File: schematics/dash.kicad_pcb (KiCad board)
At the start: 2 copper layers, 29 parts, among them J1 BATT_CONN, J2 EXTERNAL_TRIGGER, J3 USB_OTG, SW1 SW_Push, U1 ESP-12E, U2 ch340g, U3 MCP73833, U4 HT7333, Y1 12Mhz

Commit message: [add] Shitty design to start with
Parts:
- C1, C2, C3, C4, C5, C6, C7, C9, J1, R3: moved to B.Cu
- D3: value LED_Small -> LED
- J2: value EXTERNAL_TRIGGER -> EXT_TRIG
- moved C4 59.6 mm to (129.6, 102.8)
- moved Y1 49.3 mm to (136.6, 119.0), turned to 180 degrees
- moved SW1 43.9 mm to (143.0, 113.2), turned to 90 degrees
- moved C3 38.4 mm to (131.2, 118.8), turned to 270 degrees
- moved C9 30.2 mm to (154.9, 119.8), turned to 180 degrees
- moved U2 25.0 mm to (136.2, 109.8), turned to 270 degrees
- moved J1 23.8 mm to (164.7, 112.2)
- moved C7 22.4 mm to (158.9, 109.5)
- moved R5 21.3 mm to (168.8, 98.6), turned to 180 degrees
- moved R8 20.5 mm to (160.8, 121.4)
- moved C6 20.3 mm to (136.4, 109.0), turned to 90 degrees
- moved D3 20.1 mm to (129.7, 98.0), turned to 180 degrees
- moved D2 19.4 mm to (129.6, 100.5), turned to 180 degrees
- moved D1 19.0 mm to (129.6, 102.9), turned to 180 degrees
- moved C1 18.4 mm to (158.9, 112.9), turned to 180 degrees
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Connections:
- net /USB_VCC renamed +5V
- net /VCC renamed +3V3
- R3 pad 1: Net-(R3-Pad1) -> GND
- R3 pad 2: GND -> Net-(R3-Pad2)
- R4 pad 1: GND -> Net-(D3-Pad1)
- R4 pad 2: Net-(D3-Pad1) -> GND
- U3 pad 6: Net-(R3-Pad1) -> Net-(R3-Pad2)
- U3 pad 9: Net-(C1-Pad1) -> Net-(U3-Pad9)
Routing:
- net /WAKE: track 0.00 -> 40.2 mm, vias 0 -> 2
- net Net-(C1-Pad1): track 0.00 -> 35.9 mm, vias 0 -> 1
- net /CH_PD: track 0.00 -> 31.2 mm, vias 0 -> 4
- net +5V: track 0.00 -> 26.9 mm, vias 0 -> 2
- net Net-(D3-Pad2): track 0.00 -> 24.1 mm, vias 0 -> 2
- net /GPIO0: track 0.00 -> 23.2 mm, vias 0 -> 2
- net GND: track 0.00 -> 20.6 mm, vias 0 -> 4
- net Net-(C2-Pad1): track 0.00 -> 18.2 mm, vias 0 -> 3
- net (no net): track 0.00 -> 15.2 mm
- net Net-(C3-Pad1): track 0.00 -> 8.64 mm, vias 0 -> 1
- net +3V3: track 0.00 -> 8.44 mm, vias 0 -> 1
- net Net-(R3-Pad2): track 0.00 -> 7.55 mm, vias 0 -> 1
- net /D-: track 0.00 -> 6.20 mm, vias 0 -> 2
- net /GPIO2: track 0.00 -> 5.35 mm
- net Net-(R1-Pad2): track 0.00 -> 4.95 mm
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- added copper zone on F.Cu, net +3V3
- added copper zone on B.Cu, net GND
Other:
- board outline added: 50 x 30 mm

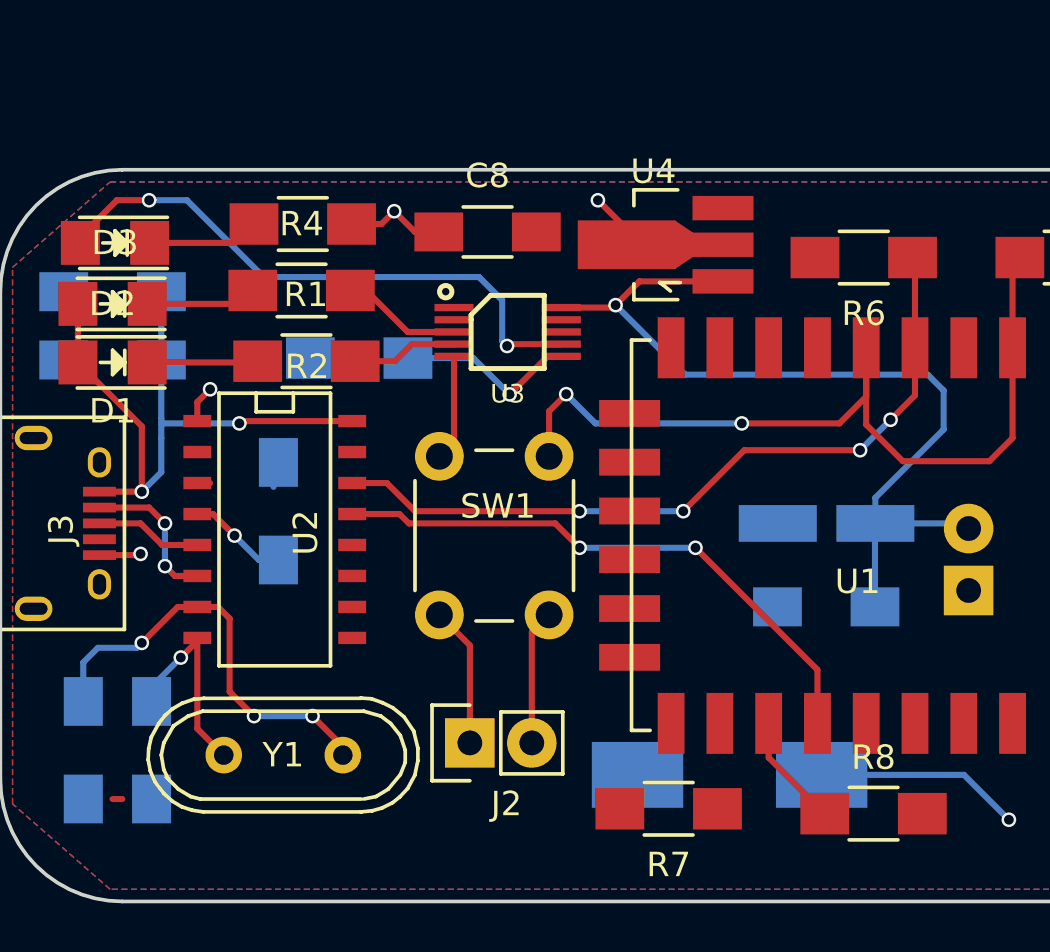
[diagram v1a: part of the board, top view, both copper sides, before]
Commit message: [enh] Change crystal placement and size
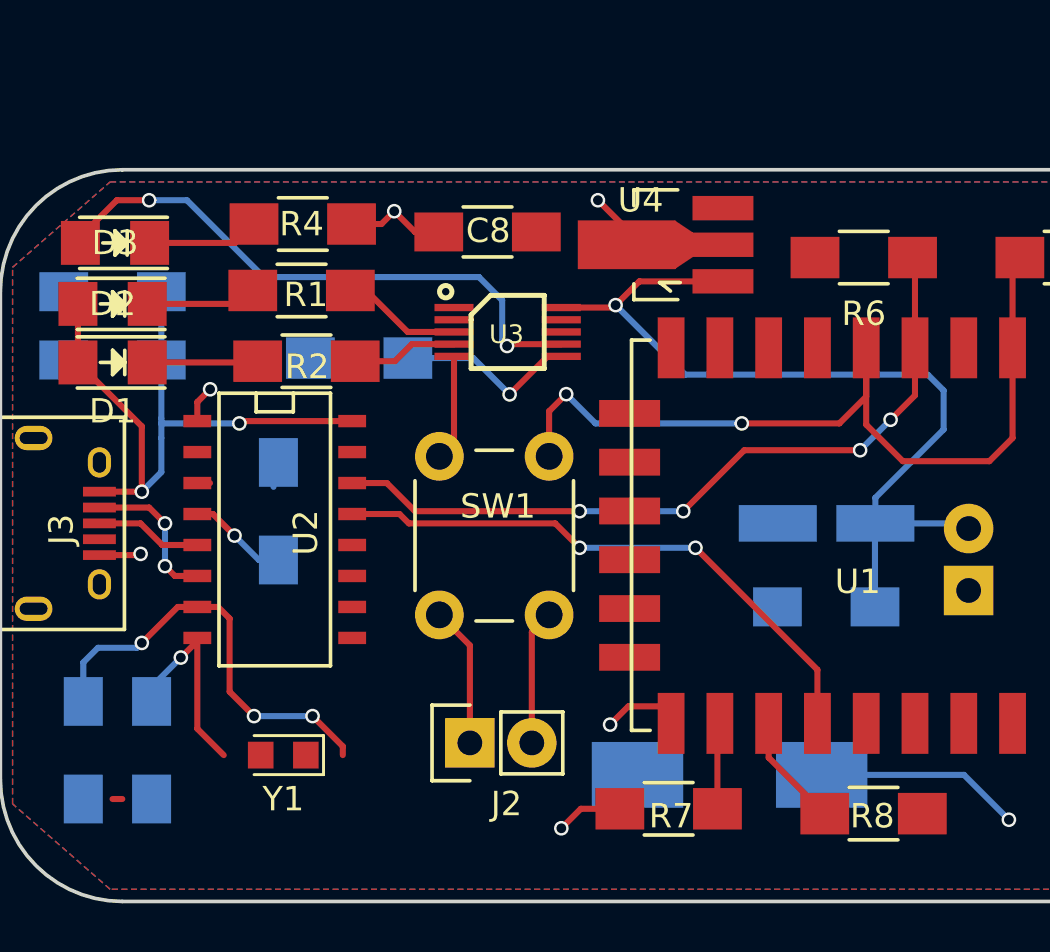
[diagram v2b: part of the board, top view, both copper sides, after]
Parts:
- J2: value EXT_TRIG -> EXTERNAL_TRIGGER
- Y1: footprint Crystals:Crystal_HC49-U_Vertical -> Crystals:Crystal_SMD_2012-2pin_2.0x1.2mm_HandSoldering
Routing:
- net GND: track 20.6 -> 26.1 mm, vias 4 -> 6
- net /GPIO15: track 0.14 -> 4.38 mm

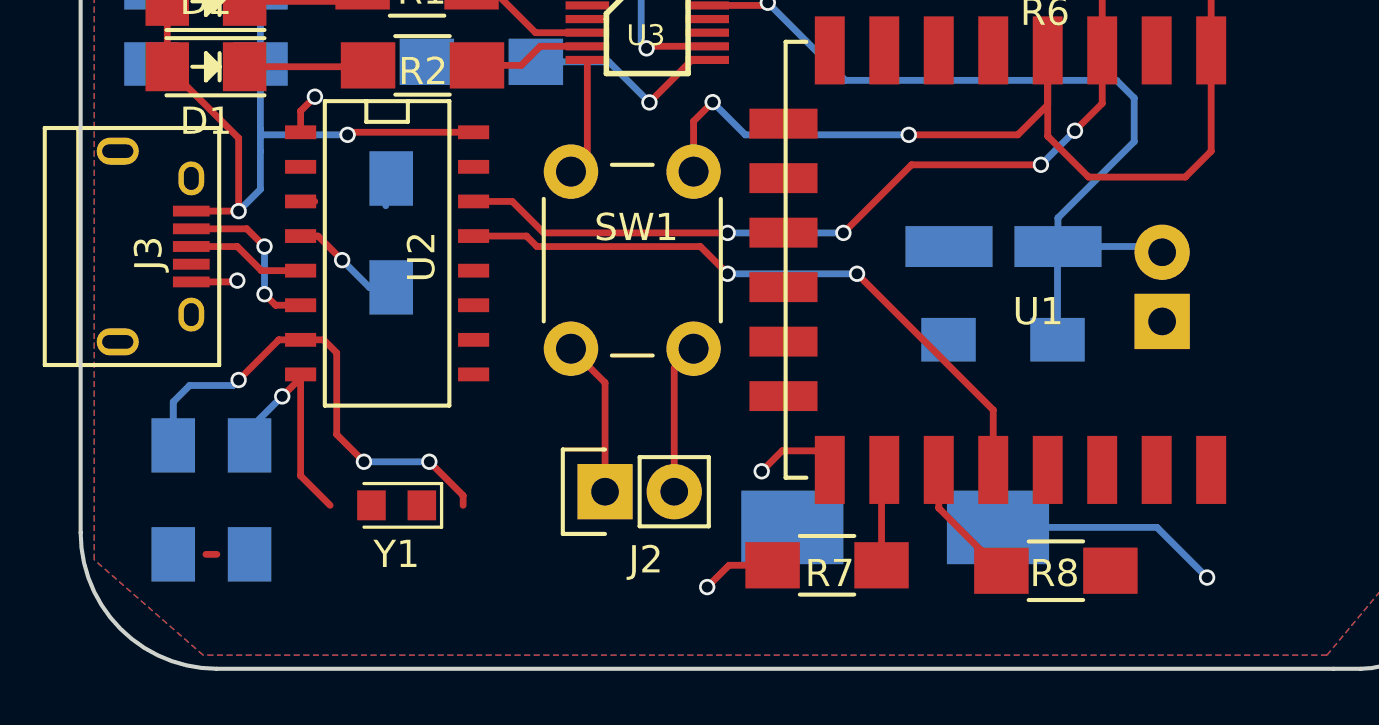
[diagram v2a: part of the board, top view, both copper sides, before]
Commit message: [add] TX/RX wiring to the ESP-12
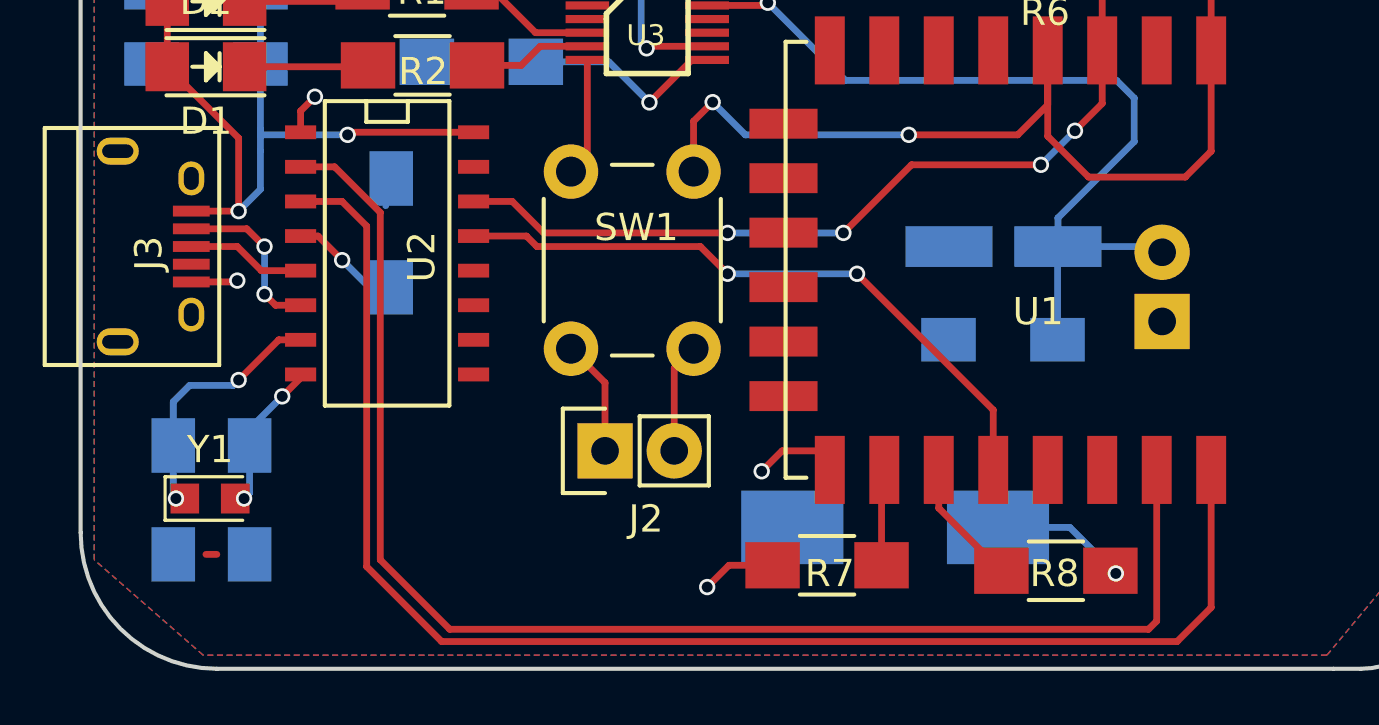
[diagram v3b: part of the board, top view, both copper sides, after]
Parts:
- moved Y1 6.85 mm to (129.8, 118.8), turned to 0 degrees
- moved J2 1.50 mm to (144.2, 117.0)
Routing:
- net /TXD: track 0.52 -> 54.2 mm
- net /RXD: track 0.00 -> 52.3 mm
- net Net-(C2-Pad1): track 18.2 -> 10.0 mm, vias 3 -> 2
- net +3V3: track 8.44 -> 5.27 mm
- net Net-(C3-Pad1): track 8.64 -> 5.89 mm, vias 1 -> 2
- net GND: track 26.1 -> 24.6 mm
- net /WAKE: track 40.2 -> 38.7 mm
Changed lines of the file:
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@@
   (general
     (links 68)
-    (no_connects 15)
+    (no_connects 12)
     (area 124.924999 94.924999 175.075001 125.075001)
     (thickness 1.6)
     (drawings 10)
-    (tracks 182)
+    (tracks 196)
     (zones 0)
     (modules 29)
@@
   )
   (module Pin_Headers:Pin_Header_Straight_1x02 (layer F.Cu)
-    (at 144.25 118.5 90)
+    (at 144.25 117 90)
     (descr "Through hole pin header")
     (tags "pin header")
@@
   )
   (module Crystals:Crystal_SMD_2012-2pin_2.0x1.2mm_HandSoldering (layer F.Cu)
-    (at 136.6 119 180)
+    (at 129.75 118.75)
     (descr "SMD Crystal 2012/2 http://txccrystal.com/images/pdf/9ht11.pdf, hand-soldering, 2.0x1.2mm^2 package")
     (tags "SMD SMT crystal hand-soldering")
     (attr smd)
-    (fp_text reference Y1 (at 0 -1.8 180) (layer F.SilkS)
-      (effects (font (size 1 1) (thickness 0.15)))
-    )
-    (fp_text value 12Mhz (at 0 1.8 180) (layer F.Fab)
-      (effects (font (size 1 1) (thickness 0.15)))
-    )
-    (fp_text user %R (at 0 0 180) (layer F.Fab)
+    (fp_text reference Y1 (at 0 -1.8) (layer F.SilkS)
+      (effects (font (size 1 1) (thickness 0.15)))
+    )
+    (fp_text value 12Mhz (at 0 1.8) (layer F.Fab)
+      (effects (font (size 1 1) (thickness 0.15)))
+    )
+    (fp_text user %R (at 0 0) (layer F.Fab)
       (effects (font (size 0.5 0.5) (thickness 0.075)))
     )
@@
     (fp_circle (center 0 0) (end 0.106667 0) (layer F.Adhes) (width 0.066667))
     (fp_circle (center 0 0) (end 0.046667 0) (layer F.Adhes) (width 0.093333))
-    (pad 1 smd rect (at -0.925 0 180) (size 1.05 1.1) (layers F.Cu F.Paste F.Mask)
+    (pad 1 smd rect (at -0.925 0) (size 1.05 1.1) (layers F.Cu F.Paste F.Mask)
       (net 3 "Net-(C2-Pad1)"))
-    (pad 2 smd rect (at 0.925 0 180) (size 1.05 1.1) (layers F.Cu F.Paste F.Mask)
+    (pad 2 smd rect (at 0.925 0) (size 1.05 1.1) (layers F.Cu F.Paste F.Mask)
       (net 4 "Net-(C3-Pad1)"))
     (model ${KISYS3DMOD}/Crystals.3dshapes/Crystal_SMD_2012-2pin_2.0x1.2mm_HandSoldering.wrl
@@
   (via (at 133.6 104) (size 0.6) (drill 0.4) (layers F.Cu B.Cu) (net 2))
   (segment (start 133.075 104.525) (end 133.6 104) (width 0.25) (layer F.Cu) (net 2))
-  (segment (start 144.25 118.5) (end 144.25 114.5) (width 0.25) (layer F.Cu) (net 2))
+  (segment (start 144.25 117) (end 144.25 114.5) (width 0.25) (layer F.Cu) (net 2) (status 10))
   (segment (start 144.25 114.5) (end 143 113.25) (width 0.25) (layer F.Cu) (net 2))
   (segment (start 129.06254 110.7991) (end 130.7009 110.7991) (width 0.25) (layer F.Cu) (net 2))
@@
   (segment (start 130.7009 110.7991) (end 130.75 110.75) (width 0.25) (layer F.Cu) (net 2))
   (segment (start 136.2 107.2) (end 136.2 108) (width 0.25) (layer B.Cu) (net 2))
+  (segment (start 128.4 116.8) (end 128.4 118.65) (width 0.25) (layer B.Cu) (net 3))
+  (segment (start 128.5 118.75) (end 128.825 118.75) (width 0.25) (layer F.Cu) (net 3))
+  (via (at 128.5 118.75) (size 0.6) (drill 0.4) (layers F.Cu B.Cu) (net 3))
+  (segment (start 128.4 118.65) (end 128.5 118.75) (width 0.25) (layer B.Cu) (net 3))
   (segment (start 133.075 112.925) (end 132.275 112.925) (width 0.25) (layer F.Cu) (net 3))
   (segment (start 128.4 115.2) (end 128.4 116.8) (width 0.25) (layer B.Cu) (net 3))
@@
   (segment (start 132.275 112.925) (end 130.8 114.4) (width 0.25) (layer F.Cu) (net 3))
   (segment (start 133.075 112.925) (end 132.675 112.925) (width 0.25) (layer F.Cu) (net 3))
-  (segment (start 133.075 112.925) (end 133.925 112.925) (width 0.25) (layer F.Cu) (net 3))
-  (segment (start 137.8 117.4) (end 139.04094 118.64094) (width 0.25) (layer F.Cu) (net 3))
-  (via (at 137.8 117.4) (size 0.6) (drill 0.4) (layers F.Cu B.Cu) (net 3))
-  (segment (start 135.4 117.4) (end 137.8 117.4) (width 0.25) (layer B.Cu) (net 3))
-  (via (at 135.4 117.4) (size 0.6) (drill 0.4) (layers F.Cu B.Cu) (net 3))
-  (segment (start 134.4 116.4) (end 135.4 117.4) (width 0.25) (layer F.Cu) (net 3))
-  (segment (start 134.4 113.4) (end 134.4 116.4) (width 0.25) (layer F.Cu) (net 3))
-  (segment (start 133.925 112.925) (end 134.4 113.4) (width 0.25) (layer F.Cu) (net 3))
-  (segment (start 139.04094 118.64094) (end 139.04094 119) (width 0.25) (layer F.Cu) (net 3))
   (segment (start 133.15 113) (end 133.075 112.925) (width 0.25) (layer F.Cu) (net 3))
+  (segment (start 131.2 116.8) (end 131.2 118.55) (width 0.25) (layer B.Cu) (net 4))
+  (segment (start 131 118.75) (end 130.675 118.75) (width 0.25) (layer F.Cu) (net 4))
+  (via (at 131 118.75) (size 0.6) (drill 0.4) (layers F.Cu B.Cu) (net 4))
+  (segment (start 131.2 118.55) (end 131 118.75) (width 0.25) (layer B.Cu) (net 4))
+  (segment (start 131.2 116.95) (end 131.2 116.8) (width 0.25) (layer B.Cu) (net 4))
   (segment (start 133.075 114.195) (end 133.075 114.325) (width 0.25) (layer F.Cu) (net 4))
   (segment (start 133.075 114.325) (end 132.4 115) (width 0.25) (layer F.Cu) (net 4))
@@
   (via (at 132.4 115) (size 0.6) (drill 0.4) (layers F.Cu B.Cu) (net 4))
   (segment (start 131.2 116.2) (end 131.2 116.8) (width 0.25) (layer B.Cu) (net 4))
-  (segment (start 133.075 114.195) (end 133.075 117.91594) (width 0.25) (layer F.Cu) (net 4))
-  (segment (start 133.075 117.91594) (end 134.15906 119) (width 0.25) (layer F.Cu) (net 4))
   (segment (start 136.4 111) (end 135.6 111) (width 0.25) (layer B.Cu) (net 5))
   (segment (start 135.6 111) (end 134.6 110) (width 0.25) (layer B.Cu) (net 5))
@@
   (segment (start 166.4 102.9) (end 166.5 103) (width 0.25) (layer F.Cu) (net 10))
   (segment (start 166.4 103.1) (end 166.5 103) (width 0.25) (layer F.Cu) (net 10))
-  (segment (start 146.79 118.5) (end 146.79 113.96) (width 0.25) (layer F.Cu) (net 10))
+  (segment (start 146.79 117) (end 146.79 113.96) (width 0.25) (layer F.Cu) (net 10) (status 10))
   (segment (start 146.79 113.96) (end 147.5 113.25) (width 0.25) (layer F.Cu) (net 10))
   (segment (start 129.06254 108.8491) (end 131.0991 108.8491) (width 0.25) (layer F.Cu) (net 11))
@@
   (segment (start 141.75 109.5) (end 147.75 109.5) (width 0.25) (layer F.Cu) (net 24))
   (segment (start 141.365 109.115) (end 141.75 109.5) (width 0.25) (layer F.Cu) (net 24))
+  (segment (start 133.075 106.575) (end 134.325 106.575) (width 0.25) (layer F.Cu) (net 27))
+  (segment (start 164.5 123.25) (end 164.5 117) (width 0.25) (layer F.Cu) (net 27))
+  (segment (start 164.200002 123.549998) (end 164.5 123.25) (width 0.25) (layer F.Cu) (net 27))
+  (segment (start 138.549998 123.549998) (end 164.200002 123.549998) (width 0.25) (layer F.Cu) (net 27))
+  (segment (start 136 121) (end 138.549998 123.549998) (width 0.25) (layer F.Cu) (net 27))
+  (segment (start 136 108.25) (end 136 121) (width 0.25) (layer F.Cu) (net 27))
+  (segment (start 134.325 106.575) (end 136 108.25) (width 0.25) (layer F.Cu) (net 27))
+  (segment (start 166.5 117) (end 166.5 122.75) (width 0.25) (layer F.Cu) (net 28))
+  (segment (start 134.595 107.845) (end 133.075 107.845) (width 0.25) (layer F.Cu) (net 28))
+  (segment (start 135.5 108.75) (end 134.595 107.845) (width 0.25) (layer F.Cu) (net 28))
+  (segment (start 135.5 121.25) (end 135.5 108.75) (width 0.25) (layer F.Cu) (net 28))
+  (segment (start 138.25 124) (end 135.5 121.25) (width 0.25) (layer F.Cu) (net 28))
+  (segment (start 165.25 124) (end 138.25 124) (width 0.25) (layer F.Cu) (net 28))
+  (segment (start 166.5 122.75) (end 165.25 124) (width 0.25) (layer F.Cu) (net 28))
   (segment (start 133.075 107.845) (end 133.595 107.845) (width 0.25) (layer F.Cu) (net 28))
   (segment (start 128.18014 102.9) (end 128.18014 100.5) (width 0.25) (layer F.Cu) (net 35))
@@
   (via (at 130.8 108.2) (size 0.6) (drill 0.4) (layers F.Cu B.Cu) (net 35))
   (segment (start 130.7991 108.1991) (end 130.8 108.2) (width 0.25) (layer F.Cu) (net 35))
-  (segment (start 158.675 119.81) (end 164.51 119.81) (width 0.25) (layer B.Cu) (net 36))
-  (via (at 166.35 121.65) (size 0.6) (drill 0.4) (layers F.Cu B.Cu) (net 36))
-  (segment (start 164.51 119.81) (end 166.35 121.65) (width 0.25) (layer B.Cu) (net 36))
+  (segment (start 158.675 119.81) (end 161.31 119.81) (width 0.25) (layer B.Cu) (net 36))
+  (segment (start 163 121.5) (end 162.9 121.4) (width 0.25) (layer F.Cu) (net 36))
+  (via (at 163 121.5) (size 0.6) (drill 0.4) (layers F.Cu B.Cu) (net 36))
+  (segment (start 161.31 119.81) (end 163 121.5) (width 0.25) (layer B.Cu) (net 36))
+  (segment (start 162.9 121.4) (end 162.8 121.4) (width 0.25) (layer F.Cu) (net 36))
   (segment (start 141.71 102.72) (end 144.39 102.72) (width 0.25) (layer B.Cu) (net 37))
   (segment (start 145.88 104.21) (end 147.44 102.65) (width 0.25) (layer F.Cu) (net 37))
